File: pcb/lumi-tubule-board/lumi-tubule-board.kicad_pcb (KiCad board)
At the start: 2 copper layers, 80 x 80 mm, 72 parts, among them Q1 DMN1045UFR4, Q10 DMN1045UFR4, Q11 DMN1045UFR4, Q12 DMN1045UFR4, Q13 DMN1045UFR4, Q2 DMN1045UFR4, Q3 DMN1045UFR4, Q4 DMN1045UFR4, Q5 DMN1045UFR4, Q6 DMN1045UFR4, Q7 DMN1045UFR4, Q8 DMN1045UFR4, Q9 DMN1045UFR4, SW1 SWITCH_TACT_SMT4.6X2.8, SW2 SWITCH_TACT_SMT4.6X2.8, U1 SHTC3, U2 VREG_SOT23-5, U3 ESP32-S3-MINI-1, U4 LIS2Dx12, X1 USB_C

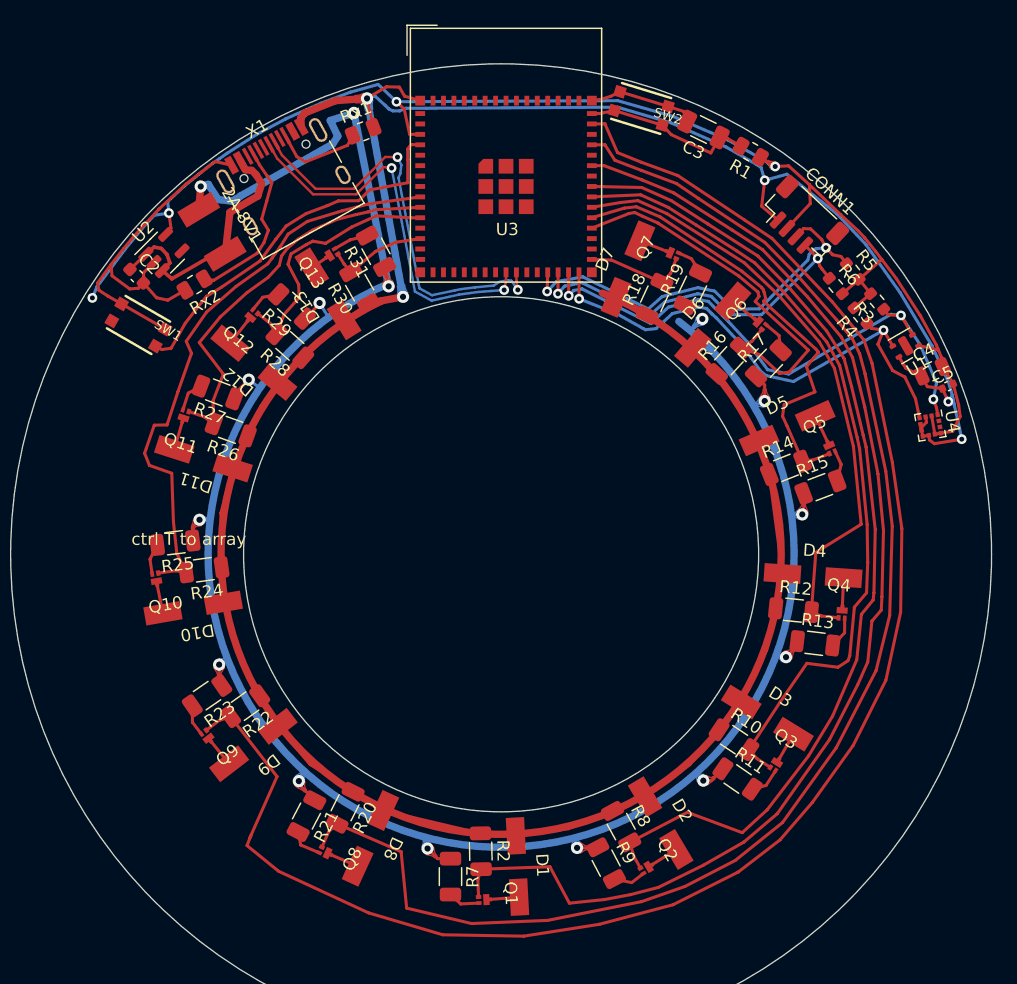
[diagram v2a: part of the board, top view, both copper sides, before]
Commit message: Revise PCB
- fixed backwards USB port
- redo power routing
- make I2C lines cleaner
- make differential lines length matched
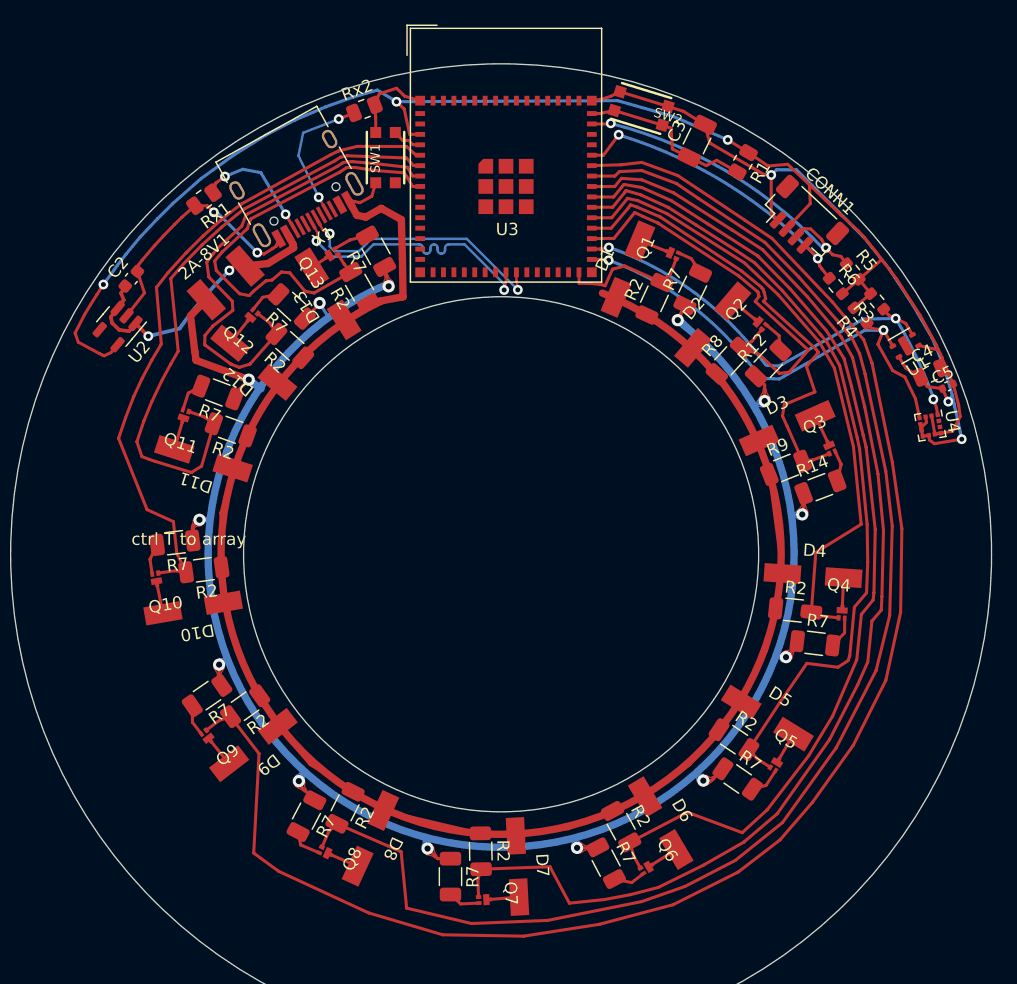
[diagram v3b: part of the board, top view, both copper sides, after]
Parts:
- moved SW1 24.3 mm to (140.6, 67.6), turned to 90 degrees
- moved Rx2 19.9 mm to (138.9, 63.7), turned to 21 degrees
- moved Rx1 14.1 mm to (125.8, 71.0), turned to -144 degrees
- moved U2 7.12 mm to (118.7, 81.4), turned to -130 degrees
- moved 2A-8V1 4.31 mm to (127.5, 77.9), turned to 41 degrees
- moved X1 1.08 mm to (132.7, 69.1), turned to -151 degrees
- moved C3 1.07 mm to (166.0, 66.3), turned to 64 degrees
- moved R1 1.07 mm to (169.7, 68.0), turned to -120 degrees
- moved C2 0.49 mm to (119.8, 77.5), turned to 50 degrees
- moved C4 0.16 mm to (185.0, 85.2)
- renumbered D7 to D1, D6 to D2, D5 to D3, D3 to D5, D2 to D6, D1 to D7, Q7 to Q1, Q6 to Q2, Q5 to Q3, Q3 to Q5, Q2 to Q6, Q1 to Q7, R17 to R12, R15 to R14, R20 to R2, R26 to R2, R30 to R2, R24 to R2, R8 to R2, R12 to R2, R22 to R2, R10 to R2, R28 to R2, R18 to R2, R13 to R7, R23 to R7, R31 to R7, R21 to R7, R11 to R7, R9 to R7, R27 to R7, R29 to R7, R19 to R7, R25 to R7, R16 to R8, R14 to R9
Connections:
- R3 pad 1: SCL_int -> SDA_int
- R4 pad 1: SDA_int -> SCL_int
- U3 pad 1: Net-(U3-Pad1) -> GND
- U3 pad 10: L11 -> unconnected-(U3-Pad10)
- U3 pad 11: L12 -> unconnected-(U3-Pad11)
- U3 pad 12: (no net) -> unconnected-(U3-Pad12)
- U3 pad 13: L13 -> unconnected-(U3-Pad13)
- U3 pad 14: (no net) -> unconnected-(U3-Pad14)
- U3 pad 15: (no net) -> unconnected-(U3-Pad15)
- U3 pad 16: (no net) -> unconnected-(U3-Pad16)
- U3 pad 17: (no net) -> unconnected-(U3-Pad17)
- U3 pad 19: SDA -> unconnected-(U3-Pad19)
- U3 pad 2: Net-(U3-Pad1) -> GND
- U3 pad 20: SCL -> unconnected-(U3-Pad20)
- U3 pad 27: SDA -> unconnected-(U3-Pad27)
- U3 pad 28: SCL -> unconnected-(U3-Pad28)
- U3 pad 29: SCL_int -> unconnected-(U3-Pad29)
- U3 pad 30: SDA_int -> L1
- U3 pad 31: L1 -> SDA_int
- U3 pad 32: (no net) -> SCL_int
- U3 pad 33: (no net) -> L2
- U3 pad 34: L2 -> L3
- U3 pad 35: L3 -> L4
- U3 pad 36: L4 -> L5
- U3 pad 37: L5 -> L6
- U3 pad 38: L6 -> L7
- U3 pad 39: (no net) -> L8
- U3 pad 40: L7 -> L9
- U3 pad 41: unconnected-(U3-Pad41) -> SCL
- U3 pad 42: L8 -> GND
- U3 pad 43: Net-(U3-Pad1) -> GND
- U3 pad 44: L9 -> SDA
- U3 pad 46: Net-(U3-Pad1) -> GND
- U3 pad 47: Net-(U3-Pad1) -> GND
- U3 pad 48: Net-(U3-Pad1) -> GND
- U3 pad 49: Net-(U3-Pad1) -> GND
- U3 pad 5: (no net) -> L10
- U3 pad 50: Net-(U3-Pad1) -> GND
- U3 pad 51: Net-(U3-Pad1) -> GND
- U3 pad 52: Net-(U3-Pad1) -> GND
- U3 pad 53: Net-(U3-Pad1) -> GND
- U3 pad 54: Net-(U3-Pad1) -> GND
- U3 pad 55: Net-(U3-Pad1) -> GND
- U3 pad 56: Net-(U3-Pad1) -> GND
- U3 pad 57: Net-(U3-Pad1) -> GND
- U3 pad 58: Net-(U3-Pad1) -> GND
- U3 pad 59: Net-(U3-Pad1) -> GND
- U3 pad 6: (no net) -> L11
- U3 pad 60: Net-(U3-Pad1) -> GND
- U3 pad 63: Net-(U3-Pad1) -> GND
- U3 pad 64: Net-(U3-Pad1) -> GND
- U3 pad 7: (no net) -> L12
- U3 pad 8: (no net) -> L13
- U3 pad 9: L10 -> unconnected-(U3-Pad9)
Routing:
- net GND: track 277.6 -> 230.9 mm
- net SCL_int: track 46.8 -> 17.5 mm
- net L13: track 8.27 -> 36.4 mm
- net Net-(SW1-PadB'): track 30.1 -> 2.45 mm
- net SDA: track 34.3 -> 7.28 mm
- net SCL: track 30.3 -> 6.50 mm
- net 5V-fused: track 193.5 -> 171.6 mm, vias 15 -> 13
- net SDA_int: track 43.2 -> 24.0 mm
- net L11: track 32.0 -> 50.5 mm
- net L12: track 21.1 -> 39.2 mm
- net D+: track 34.1 -> 21.9 mm
- net D-: track 32.1 -> 23.3 mm
- net L10: track 47.8 -> 54.1 mm
- net /3.3V: track 116.0 -> 119.5 mm, vias 4 -> 3
- net L9: track 135.1 -> 132.0 mm
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
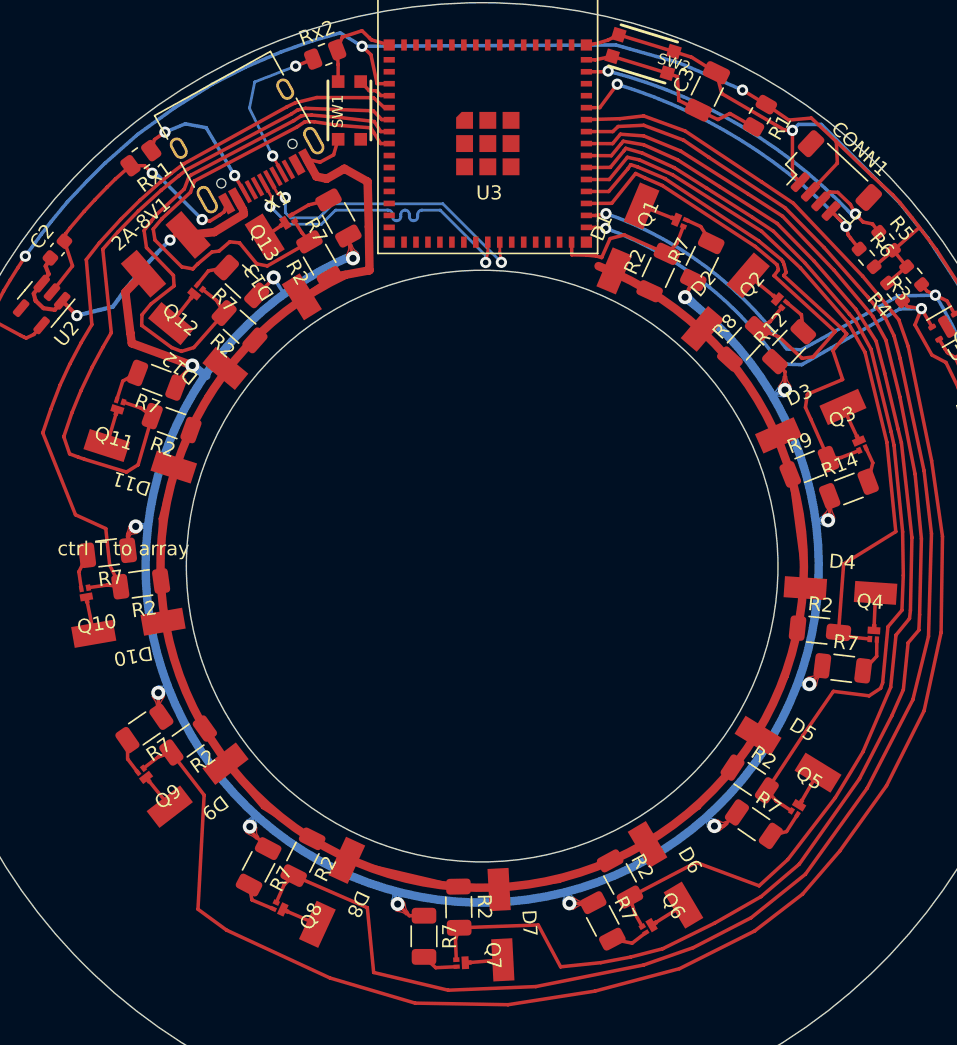
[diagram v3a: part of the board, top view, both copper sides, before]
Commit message: Add LED and fix pad numbers
Add low power LED to board and fix some missing links between schematic and pcb design.
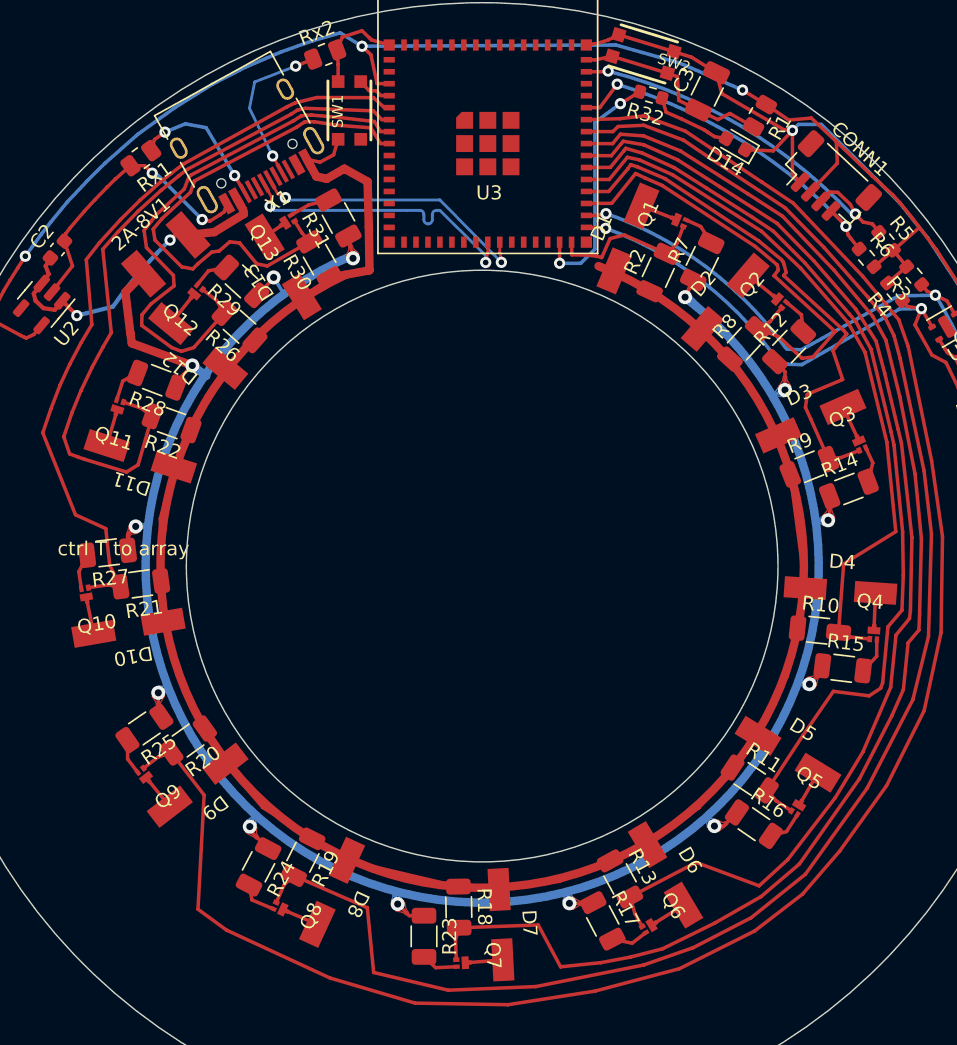
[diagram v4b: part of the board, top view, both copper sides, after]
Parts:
- added D14: LED, LED_SMD:LED_0603_1608Metric, F.Cu at (168.0, 70.0)
- added R32: 5.1k, Resistor_SMD:R_0603_1608Metric, F.Cu at (162.0, 66.6)
- renumbered R2 to R10, R2 to R11, R2 to R13, R7 to R15, R7 to R16, R7 to R17, R2 to R18, R2 to R19, R2 to R20, R2 to R21, R2 to R22, R7 to R23, R7 to R24, R7 to R25, R2 to R26, R7 to R27, R7 to R28, R7 to R29, R2 to R30, R7 to R31
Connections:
- D10 pad 2: Net-(D1-Pad2) -> Net-(D10-Pad2)
- D11 pad 2: Net-(D1-Pad2) -> Net-(D11-Pad2)
- D12 pad 2: Net-(D1-Pad2) -> Net-(D12-Pad2)
- D13 pad 2: Net-(D1-Pad2) -> Net-(D13-Pad2)
- D2 pad 2: Net-(D1-Pad2) -> Net-(D2-Pad2)
- D3 pad 2: Net-(D1-Pad2) -> Net-(D3-Pad2)
- D4 pad 2: Net-(D1-Pad2) -> Net-(D4-Pad2)
- D5 pad 2: Net-(D1-Pad2) -> Net-(D5-Pad2)
- D6 pad 2: Net-(D1-Pad2) -> Net-(D6-Pad2)
- D7 pad 2: Net-(D1-Pad2) -> Net-(D7-Pad2)
- D8 pad 2: Net-(D1-Pad2) -> Net-(D8-Pad2)
- D9 pad 2: Net-(D1-Pad2) -> Net-(D9-Pad2)
- Q10 pad 1: Net-(D1-Pad2) -> Net-(D10-Pad2)
- Q10 pad 3: Net-(Q1-Pad3) -> Net-(Q10-Pad3)
- Q11 pad 1: Net-(D1-Pad2) -> Net-(D11-Pad2)
- Q11 pad 3: Net-(Q1-Pad3) -> Net-(Q11-Pad3)
- Q12 pad 1: Net-(D1-Pad2) -> Net-(D12-Pad2)
- Q12 pad 3: Net-(Q1-Pad3) -> Net-(Q12-Pad3)
- Q13 pad 1: Net-(D1-Pad2) -> Net-(D13-Pad2)
- Q13 pad 3: Net-(Q1-Pad3) -> Net-(Q13-Pad3)
- Q2 pad 1: Net-(D1-Pad2) -> Net-(D2-Pad2)
- Q2 pad 3: Net-(Q1-Pad3) -> Net-(Q2-Pad3)
- Q3 pad 1: Net-(D1-Pad2) -> Net-(D3-Pad2)
- Q3 pad 3: Net-(Q1-Pad3) -> Net-(Q3-Pad3)
- Q4 pad 1: Net-(D1-Pad2) -> Net-(D4-Pad2)
- Q4 pad 3: Net-(Q1-Pad3) -> Net-(Q4-Pad3)
- Q5 pad 1: Net-(D1-Pad2) -> Net-(D5-Pad2)
- Q5 pad 3: Net-(Q1-Pad3) -> Net-(Q5-Pad3)
- Q6 pad 1: Net-(D1-Pad2) -> Net-(D6-Pad2)
- Q6 pad 3: Net-(Q1-Pad3) -> Net-(Q6-Pad3)
- Q7 pad 1: Net-(D1-Pad2) -> Net-(D7-Pad2)
- Q7 pad 3: Net-(Q1-Pad3) -> Net-(Q7-Pad3)
- Q8 pad 1: Net-(D1-Pad2) -> Net-(D8-Pad2)
- Q8 pad 3: Net-(Q1-Pad3) -> Net-(Q8-Pad3)
- Q9 pad 1: Net-(D1-Pad2) -> Net-(D9-Pad2)
- Q9 pad 3: Net-(Q1-Pad3) -> Net-(Q9-Pad3)
- R12 pad 2: Net-(Q1-Pad3) -> Net-(Q2-Pad3)
- R14 pad 2: Net-(Q1-Pad3) -> Net-(Q3-Pad3)
- R15 pad 2: Net-(Q1-Pad3) -> Net-(Q4-Pad3)
- R16 pad 2: Net-(Q1-Pad3) -> Net-(Q5-Pad3)
- R17 pad 2: Net-(Q1-Pad3) -> Net-(Q6-Pad3)
- R23 pad 2: Net-(Q1-Pad3) -> Net-(Q7-Pad3)
- R24 pad 2: Net-(Q1-Pad3) -> Net-(Q8-Pad3)
- R25 pad 2: Net-(Q1-Pad3) -> Net-(Q9-Pad3)
- R27 pad 2: Net-(Q1-Pad3) -> Net-(Q10-Pad3)
- R28 pad 2: Net-(Q1-Pad3) -> Net-(Q11-Pad3)
- R29 pad 2: Net-(Q1-Pad3) -> Net-(Q12-Pad3)
- R31 pad 2: Net-(Q1-Pad3) -> Net-(Q13-Pad3)
- U3 pad 29: unconnected-(U3-Pad29) -> LED
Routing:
- net Net-(Q1-Pad3): track 34.1 -> 2.52 mm
- net Net-(D1-Pad2): track 32.4 -> 2.67 mm
- net LED: track 0.00 -> 17.3 mm, vias 0 -> 2
- net Net-(D14-Pad2): track 0.00 -> 5.73 mm
- net GND: track 230.9 -> 234.9 mm
- net Net-(Q13-Pad3): track 0.00 -> 2.91 mm
- net Net-(Q8-Pad3): track 0.00 -> 2.72 mm
- net Net-(D2-Pad2): track 0.00 -> 2.67 mm
- net Net-(D3-Pad2): track 0.00 -> 2.67 mm
- net Net-(D12-Pad2): track 0.00 -> 2.67 mm
- net Net-(D4-Pad2): track 0.00 -> 2.67 mm
- net Net-(D9-Pad2): track 0.00 -> 2.67 mm
- net Net-(D6-Pad2): track 0.00 -> 2.67 mm
- net Net-(D11-Pad2): track 0.00 -> 2.67 mm
- net Net-(Q6-Pad3): track 0.00 -> 2.66 mm
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
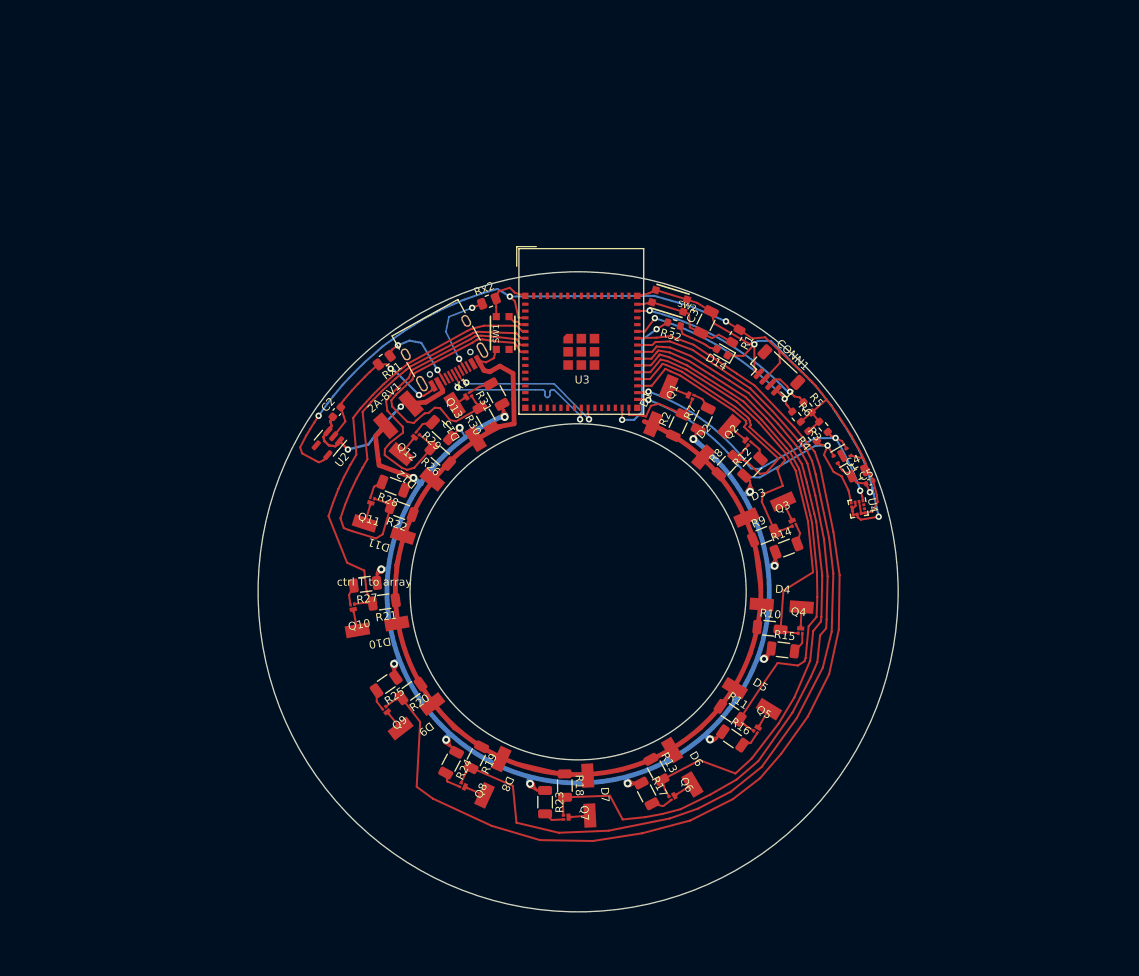
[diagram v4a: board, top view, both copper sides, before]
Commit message: Move to ground plane approach
Opt to go for ground plane design and forgo extra PCB art colour. Simplifies a lot of things. Currently I2C lines still need to be wired up and some traced cleaned up.
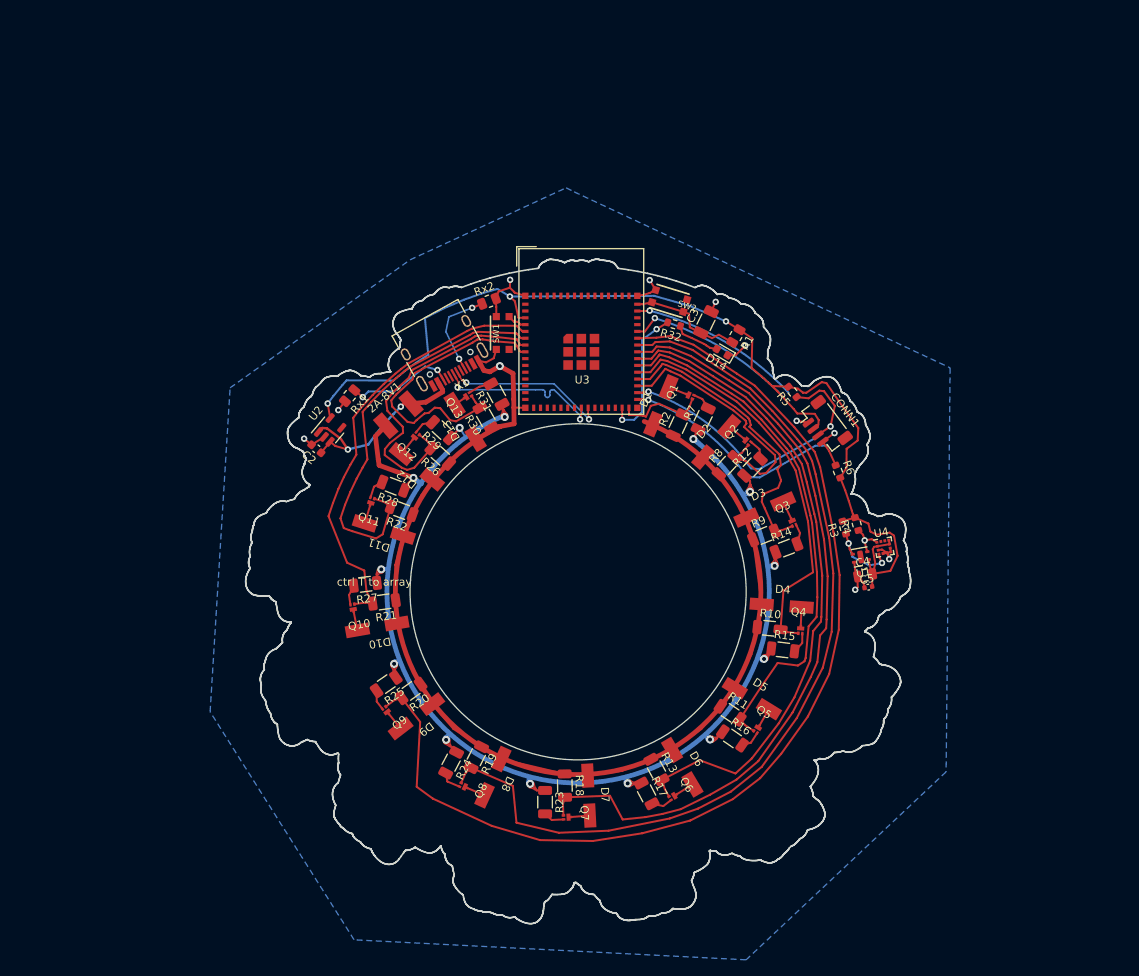
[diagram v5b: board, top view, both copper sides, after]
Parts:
- moved C5 13.1 mm to (186.3, 99.4), turned to 10 degrees
- moved U1 12.9 mm to (185.3, 95.6), turned to -170 degrees
- moved R3 12.8 mm to (183.3, 92.0), turned to 105 degrees
- moved C4 12.8 mm to (185.9, 97.9), turned to 10 degrees
- moved R4 12.3 mm to (184.8, 91.5), turned to 105 degrees
- moved CONN1 8.93 mm to (180.7, 79.3), turned to -53 degrees
- moved R6 8.59 mm to (182.5, 85.0), turned to -70 degrees
- moved Rx1 6.20 mm to (121.4, 75.5), turned to -130 degrees
- moved U4 5.88 mm to (188.2, 94.4), turned to 10 degrees
- moved C2 5.26 mm to (117.3, 82.1), turned to 140 degrees
- moved R5 2.69 mm to (176.8, 75.0), turned to 129 degrees
- moved U2 1.69 mm to (119.0, 79.8), turned to 50 degrees
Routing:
- net GND: track 234.9 -> 173.4 mm, vias 5 -> 10
- net /3.3V: track 119.5 -> 136.2 mm
- net SCL_int: track 17.5 -> 6.03 mm, vias 3 -> 2
- net SDA_int: track 24.0 -> 31.1 mm, vias 2 -> 3
- net SDA: track 7.28 -> 11.8 mm
- net Net-(Rx1-Pad1): track 10.2 -> 13.7 mm
- net Net-(2A-8V1-Pad2): track 23.4 -> 25.2 mm
- net SCL: track 6.50 -> 7.90 mm
- net L3: track 37.8 -> 36.9 mm
- added copper zone on B.Cu, net GND
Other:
- board size 80 x 80 mm -> 83.1 x 83 mm
